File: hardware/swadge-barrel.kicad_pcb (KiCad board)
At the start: 2 copper layers, 70.4 x 89.6 mm, 48 parts, among them J1 USB_B_Micro, Q1 Q_NPN_BEC, U1 ESP-13-WROOM-02D, U2 DISP_OLED_UG-2864HSWEG01, U3 BUS_PCIexpress, U4 QMA6981, U5 AP1117-33

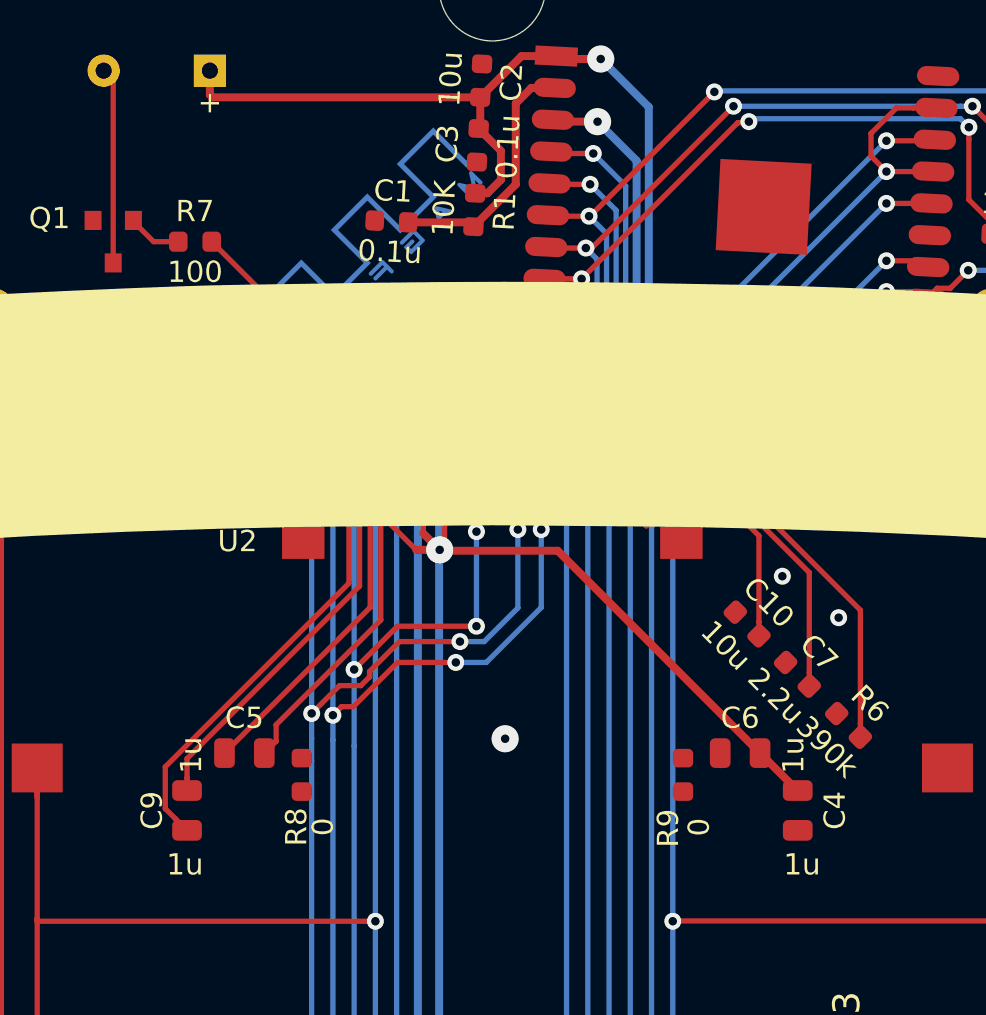
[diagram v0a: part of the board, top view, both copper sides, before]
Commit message: Replaced 0805 caps with 1206 caps
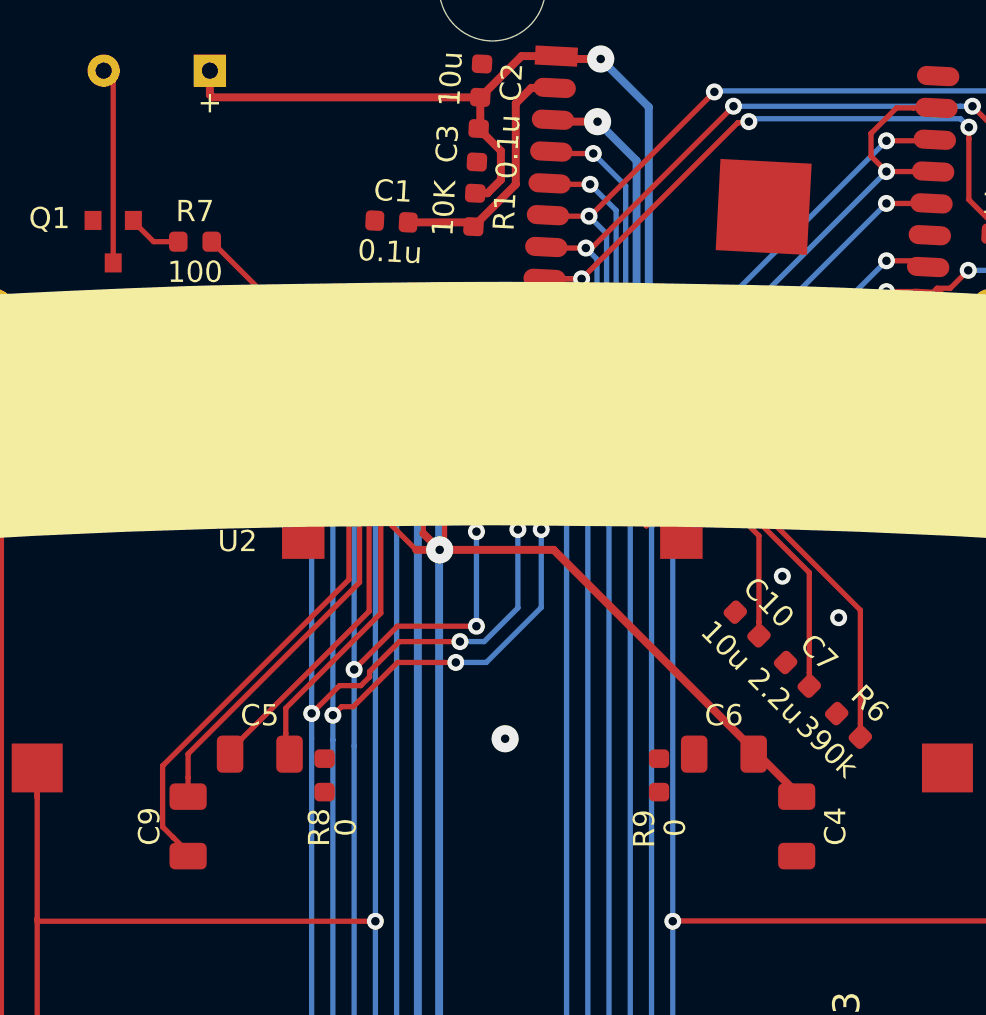
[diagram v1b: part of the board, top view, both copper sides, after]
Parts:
- removed svg2mod: G***, Swadge_Parts:MAGFEST_logo_centered_final
- C4, C5, C6, C9: footprint Swadge_Parts:C_0805_2012Metric -> Swadge_Parts:C_1206_3216Metric
- moved R9 1.13 mm to (153.3, 94.3)
- moved R8 1.08 mm to (137.6, 94.3)
- moved C6 0.76 mm to (156.4, 93.3)
- moved C4 0.75 mm to (159.8, 96.7)
- moved C9 0.75 mm to (131.2, 96.7)
- moved C5 0.73 mm to (134.6, 93.3)
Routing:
- net Net-(C9-Pad1): track 20.6 -> 21.8 mm

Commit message: Finished BOM notes
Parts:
- added U2: OLED_DISPLAY, Swadge_Parts:NULL, F.Cu at (145.9, 47.2)
- LS1: footprint Swadge_Parts:Speaker_9mm -> Swadge_Parts:Buzzer_12x9.5RM7.6
- U6: renamed from U2; value DISP_OLED_UG-2864HSWEG01 -> OLED_CONNECTOR
- moved LS1 5.23 mm to (134.9, 61.1), turned to 180 degrees
- renumbered S4 to SW1
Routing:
- net +3V3: track 308.5 -> 305.2 mm
- net Net-(LS1-Pad2): track 9.24 -> 11.9 mm
- net GND: track 88.9 -> 90.1 mm
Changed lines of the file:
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@@
     (thickness 1.6)
     (drawings 366)
-    (tracks 517)
+    (tracks 519)
     (zones 0)
-    (modules 47)
+    (modules 48)
     (nets 40)
   )
@@
   (net 37 BZR)
   (net 38 SW1)
-  (net 39 "Net-(S4-Pad3)")
+  (net 39 "Net-(SW1-Pad3)")
   (net_class Default "This is the default net class."
     (clearance 0.2)
@@
     (add_net "Net-(Q1-Pad1)")
     (add_net "Net-(R6-Pad2)")
-    (add_net "Net-(S4-Pad3)")
+    (add_net "Net-(SW1-Pad3)")
     (add_net "Net-(U3-PadA10)")
     (add_net "Net-(U3-PadA9)")
@@
     (uvia_drill 0.1)
   )
+  (module Swadge_Parts:Buzzer_12x9.5RM7.6 (layer F.Cu)
+    (at 134.925 61.075 180)
+    (descr "Generic Buzzer, D12mm height 9.5mm with RM7.6mm")
+    (tags buzzer)
+    (fp_text reference LS1 (at -1.925 5.175) (layer F.SilkS)
+      (effects (font (size 1 1) (thickness 0.15)))
+    )
+    (fp_text value Speaker (at 3.8 7.4) (layer F.Fab)
+      (effects (font (size 1 1) (thickness 0.15)))
+    )
+    (fp_circle (center 2.5 0) (end 7 0) (layer F.Fab) (width 0.1))
+    (fp_circle (center 3.8 0) (end 9.9 0) (layer F.Fab) (width 0.12))
+    (fp_circle (center 3.8 0) (end 4.8 0) (layer F.Fab) (width 0.1))
+    (fp_circle (center 3.8 0) (end 9.8 0) (layer F.Fab) (width 0.1))
+    (fp_circle (center 3.8 0) (end 10.05 0) (layer F.CrtYd) (width 0.05))
+    (fp_text user + (at -0.01 -2.54) (layer F.SilkS)
+      (effects (font (size 1 1) (thickness 0.15)))
+    )
+    (pad 2 thru_hole circle (at 5 0 180) (size 2 2) (drill 1) (layers *.Cu *.Mask)
+      (net 35 "Net-(LS1-Pad2)"))
+    (pad 2 thru_hole circle (at 7.6 0 180) (size 2 2) (drill 1) (layers *.Cu *.Mask)
+      (net 35 "Net-(LS1-Pad2)"))
+    (pad 1 thru_hole rect (at 0 0 180) (size 2 2) (drill 1) (layers *.Cu *.Mask)
+      (net 5 +3V3))
+    (model ${KIPRJMOD}/kicad-libs/package3d/Buzzer_12x9.5RM7.6.wrl
+      (at (xyz 0 0 0))
+      (scale (xyz 1 1 0.5))
+      (rotate (xyz 0 0 0))
+    )
+  )
+  (module Swadge_Parts:NULL (layer F.Cu)
+    (at 145.9 47.175)
+    (fp_text reference U2 (at -15.1 65.7) (layer F.SilkS)
+      (effects (font (size 1 1) (thickness 0.15)))
+    )
+    (fp_text value OLED_DISPLAY (at -14.7 59.525 90) (layer F.Fab) hide
+      (effects (font (size 1 1) (thickness 0.15)))
+    )
+  )
   (module Swadge_Parts:oled-flat_copy (layer F.Cu)
     (at 145.4968 93.8 180)
-    (fp_text reference U2 (at 11.9968 10.4936 180) (layer F.SilkS)
+    (fp_text reference U6 (at 11.4968 10.025 180) (layer F.SilkS)
       (effects (font (size 1 1) (thickness 0.15)))
     )
-    (fp_text value DISP_OLED_UG-2864HSWEG01 (at -10.16 -20.8286 180) (layer F.Fab)
+    (fp_text value OLED_CONNECTOR (at -10.16 -20.8286 180) (layer F.Fab)
       (effects (font (size 1 1) (thickness 0.15)))
     )
@@
     )
   )
-  (module Swadge_Parts:Speaker_9mm (layer F.Cu)
-    (at 129.7 61.15)
-    (fp_text reference LS1 (at 5.25 -4) (layer F.SilkS)
-      (effects (font (size 1 1) (thickness 0.15)))
-    )
-    (fp_text value Speaker (at 0 -5.5) (layer F.Fab)
-      (effects (font (size 1 1) (thickness 0.15)))
-    )
-    (fp_text user + (at 2.5 1.5) (layer F.SilkS)
-      (effects (font (size 1 1) (thickness 0.15)))
-    )
-    (fp_circle (center 0 0) (end 4.5 0) (layer F.Fab) (width 0.12))
-    (pad 2 thru_hole circle (at -2.5 0) (size 1.524 1.524) (drill 0.762) (layers *.Cu *.Mask)
-      (net 35 "Net-(LS1-Pad2)"))
-    (pad 1 thru_hole rect (at 2.5 0) (size 1.524 1.524) (drill 0.762) (layers *.Cu *.Mask)
-      (net 5 +3V3))
-    (model ${KIPRJMOD}/kicad-libs/package3d/Buzzer.step
-      (offset (xyz 0 0.4 0))
-      (scale (xyz 0.4 0.75 0.75))
-      (rotate (xyz 90 -90 0))
-    )
-  )
   (module Swadge_Parts:SOT-23 (layer F.Cu)
     (at 127.65 69.2 270)
@@
       (net 18 +5V))
     (pad 2 smd rect (at -3.15 0 95) (size 2 1.5) (layers F.Cu F.Paste F.Mask)
-      (net 39 "Net-(S4-Pad3)"))
+      (net 39 "Net-(SW1-Pad3)"))
     (pad 2 smd rect (at 3.15 0 95) (size 2 3.8) (layers F.Cu F.Paste F.Mask)
-      (net 39 "Net-(S4-Pad3)"))
+      (net 39 "Net-(SW1-Pad3)"))
     (model ${KIPRJMOD}/kicad-libs/package3d/SOT-223.wrl
       (at (xyz 0 0 0))
@@
     (descr "Ultraminiature Surface Mount Slide Switch")
     (attr smd)
-    (fp_text reference S4 (at 0 -3.2 355) (layer F.SilkS)
+    (fp_text reference SW1 (at 0 -3.2 355) (layer F.SilkS)
       (effects (font (size 1 1) (thickness 0.15)))
     )
@@
       (net 1 GND))
     (pad 3 smd rect (at 2.25 -1.43 355) (size 0.7 1.5) (layers F.Cu F.Paste F.Mask)
-      (net 39 "Net-(S4-Pad3)"))
+      (net 39 "Net-(SW1-Pad3)"))
     (pad 2 smd rect (at 0.75 -1.43 355) (size 0.7 1.5) (layers F.Cu F.Paste F.Mask)
       (net 5 +3V3))
@@
   (segment (start 143.7468 80.2836) (end 143.7468 78.946801) (width 0.25) (layer F.Cu) (net 1))
   (segment (start 138.2468 78.946801) (end 150.2468 78.946801) (width 0.25) (layer F.Cu) (net 1))
+  (segment (start 152.7468 80.2836) (end 154.0086 80.2836) (width 0.375) (layer F.Cu) (net 1))
   (segment (start 168.915497 72.234503) (end 169.25 71.9) (width 0.375) (layer F.Cu) (net 2))
   (segment (start 122.880999 72.953989) (end 122.116 72.18899) (width 0.375) (layer F.Cu) (net 2))
@@
   (segment (start 129.817385 124.65) (end 125.872228 120.704843) (width 0.375) (layer F.Cu) (net 5))
   (segment (start 143.0191 124.65) (end 129.817385 124.65) (width 0.375) (layer F.Cu) (net 5))
-  (segment (start 132.2 62.287) (end 132.2 61.15) (width 0.375) (layer F.Cu) (net 5))
-  (segment (start 132.319532 62.406532) (end 132.2 62.287) (width 0.375) (layer F.Cu) (net 5))
-  (segment (start 144.930405 62.406532) (end 132.319532 62.406532) (width 0.375) (layer F.Cu) (net 5))
   (segment (start 140.7468 81.3272) (end 140.7468 80.2836) (width 0.25) (layer F.Cu) (net 5))
   (segment (start 142.2468 81.2032) (end 142.2468 80.2836) (width 0.25) (layer F.Cu) (net 5))
@@
   (segment (start 148.3834 83.7084) (end 143.0191 83.7084) (width 0.375) (layer F.Cu) (net 5))
   (segment (start 158 93.325) (end 148.3834 83.7084) (width 0.375) (layer F.Cu) (net 5))
+  (segment (start 136.256532 62.406532) (end 134.925 61.075) (width 0.375) (layer F.Cu) (net 5))
+  (segment (start 144.930405 62.406532) (end 136.256532 62.406532) (width 0.375) (layer F.Cu) (net 5))
   (segment (start 135.775 92.35) (end 135.775 93.325) (width 0.25) (layer F.Cu) (net 6))
   (segment (start 135.775 91.16141) (end 135.775 92.35) (width 0.25) (layer F.Cu) (net 6))
@@
   (segment (start 129.55 69.2) (end 128.6 68.25) (width 0.25) (layer F.Cu) (net 34))
   (segment (start 130.7125 69.2) (end 129.55 69.2) (width 0.25) (layer F.Cu) (net 34))
-  (segment (start 127.65 61.6) (end 127.2 61.15) (width 0.25) (layer F.Cu) (net 35))
-  (segment (start 127.65 70.2) (end 127.65 61.6) (width 0.25) (layer F.Cu) (net 35))
+  (segment (start 127.65 61.4) (end 127.325 61.075) (width 0.25) (layer F.Cu) (net 35))
+  (segment (start 127.65 70.2) (end 127.65 61.4) (width 0.25) (layer F.Cu) (net 35))
+  (segment (start 128.739213 61.075) (end 129.925 61.075) (width 0.25) (layer F.Cu) (net 35))
+  (segment (start 127.325 61.075) (end 128.739213 61.075) (width 0.25) (layer F.Cu) (net 35))
   (via (at 147.65 115.55) (size 0.8) (drill 0.4) (layers F.Cu B.Cu) (net 36))
   (segment (start 145.9916 117.2084) (end 147.65 115.55) (width 0.25) (layer B.Cu) (net 36))
@@
     (polygon
       (pts
-        (xy 148.85 80.9) (xy 149.65 80.9) (xy 149.65 81.65) (xy 148.85 81.65)
+        (xy 137.9 79.9) (xy 153.1 79.9) (xy 153.1 80.65) (xy 137.9 80.65)
       )
     )
